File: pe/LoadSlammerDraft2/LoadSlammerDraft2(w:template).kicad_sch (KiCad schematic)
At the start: 14 parts, among them J1 Screw_Terminal_01x02, J2 Conn_Coaxial, J3 Conn_Coaxial, Q1 Q_NMOS_GDS, U1 ${SIM.PARAMS}, U2 BD50FC0FP

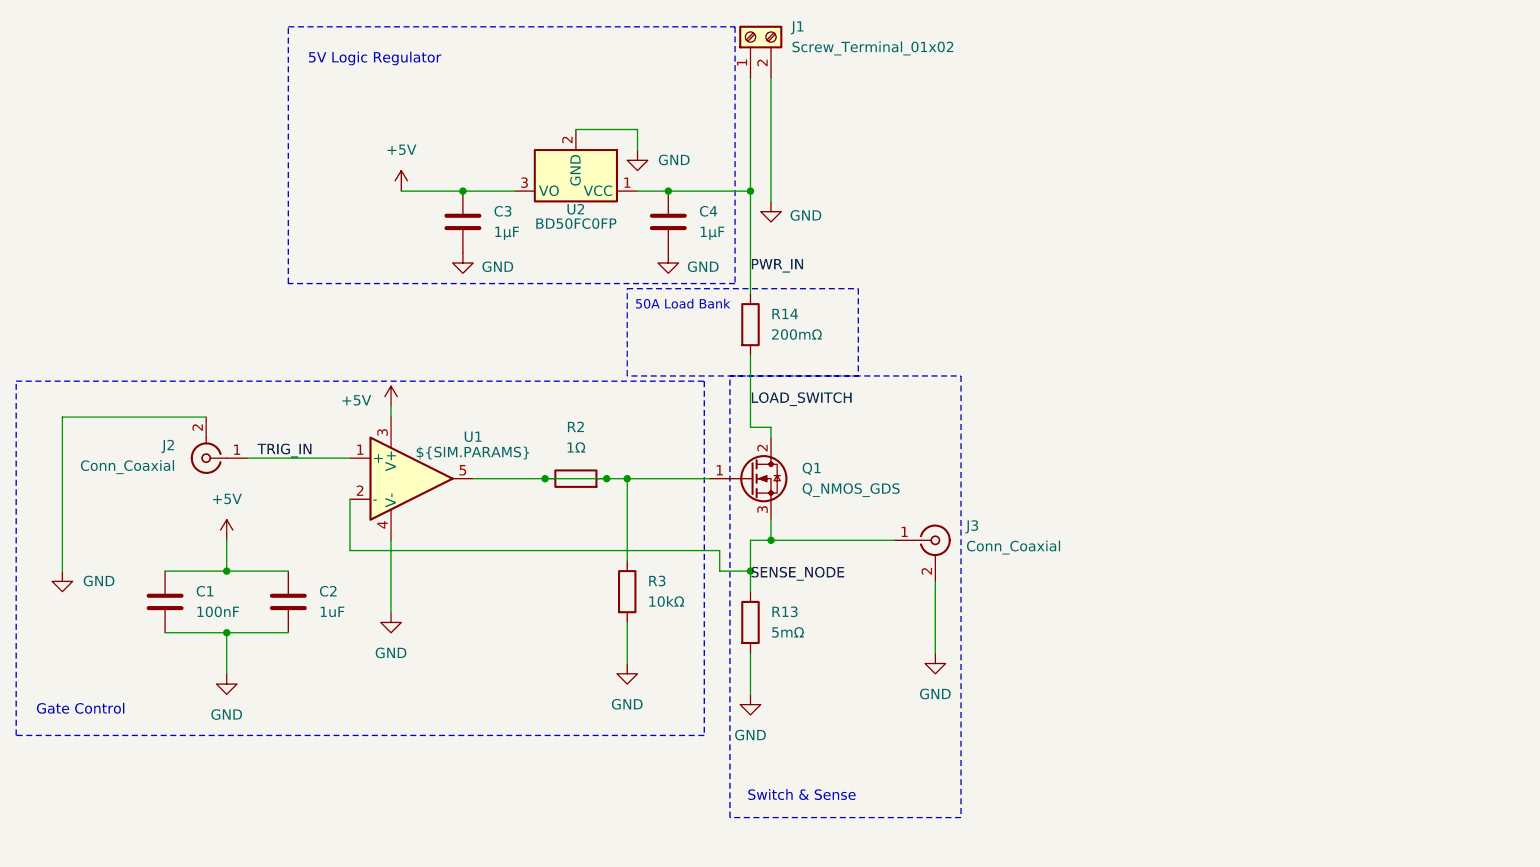
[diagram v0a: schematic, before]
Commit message: Load Slammer: cleaner schematic layout, J2/J3 changed from BNC to 2-pin headers, removed J4
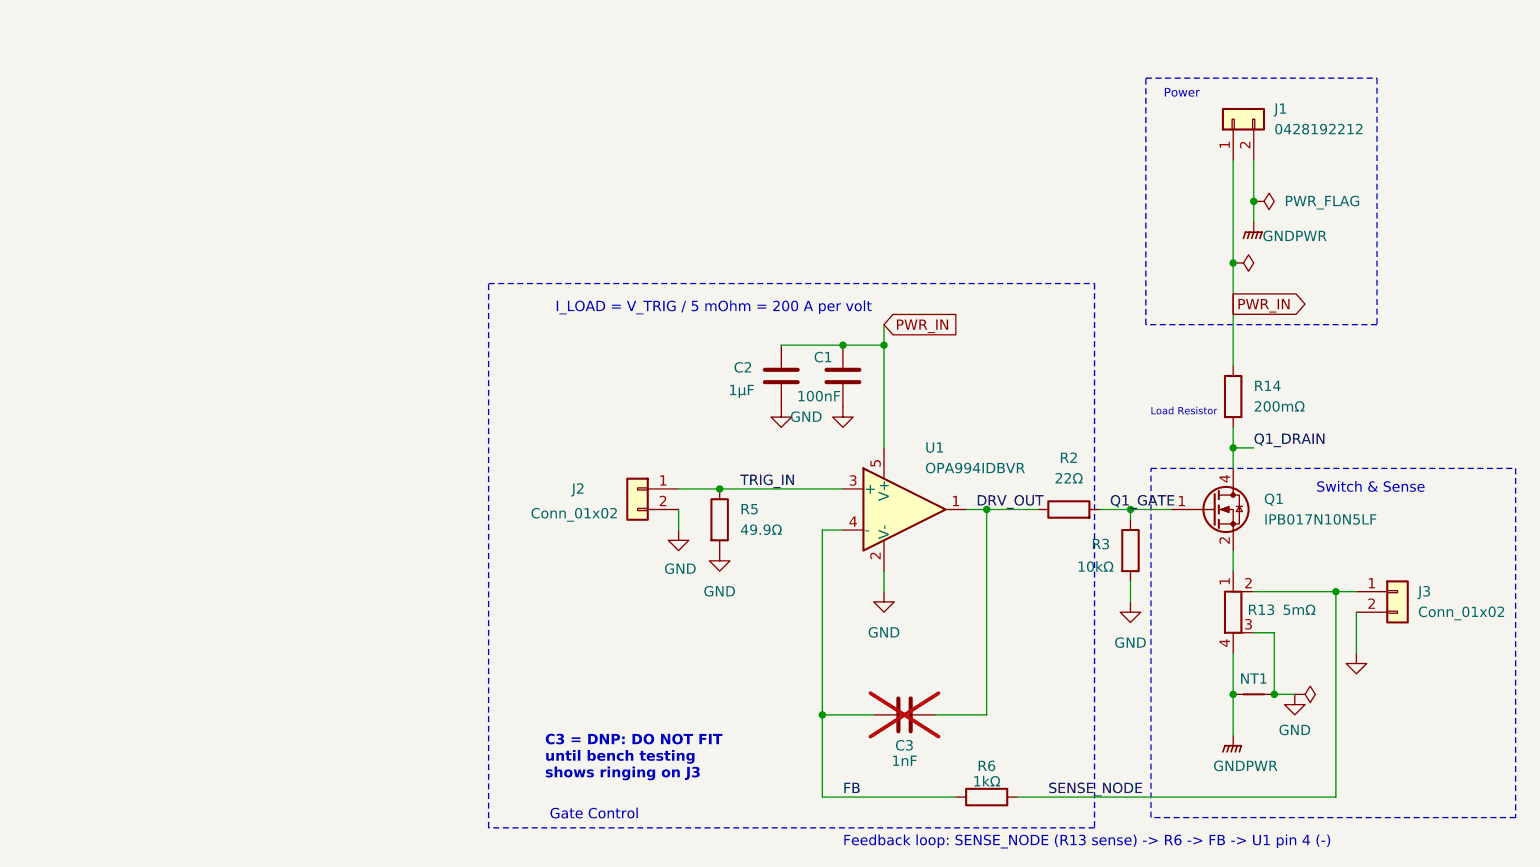
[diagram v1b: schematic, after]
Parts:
- removed C4: 1µF, Package_TO_SOT_SMD:TO-252-2, symbol Device:C
- removed U2: BD50FC0FP, Package_TO_SOT_SMD:TO-252-2, symbol Regulator_Linear:BD50FC0FP
- added NT1: NetTie_2, NetTie:NetTie-2_SMD_Pad0.5mm, symbol Device:NetTie_2
- added R5: 49.9Ω, Resistor_SMD:R_2512_6332Metric_Pad1.40x3.35mm_HandSolder, symbol Device:R
- added R6: 1kΩ, Resistor_SMD:R_0603_1608Metric_Pad0.98x0.95mm_HandSolder, symbol Device:R
- C1: footprint (none) -> Capacitor_SMD:C_0603_1608Metric_Pad1.08x0.95mm_HandSolder; Digikey Part Number (none) -> 311-1344-1-ND; Digikey URL (none) -> https://www.digikey.com/en/products/detail/yageo/CC0603KRX7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; Manufacturer (none) -> YAGEO; Manufacturer Part Number (none) -> CC0603KRX7R9BB104
- C2: value 1uF -> 1µF; footprint (none) -> Capacitor_SMD:C_0603_1608Metric_Pad1.08x0.95mm_HandSolder; Digikey Part Number (none) -> 445-CGA3E3X7R1H105K080ABCT-ND; Digikey URL (none) -> https://www.digikey.com/en/products/detail/tdk-corporation/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; Manufacturer (none) -> TDK; Manufacturer Part Number (none) -> CGA3E3X7R1H105K080AB
- C3: value 1µF -> 1nF; footprint Package_TO_SOT_SMD:TO-252-2 -> Capacitor_SMD:C_0603_1608Metric_Pad1.08x0.95mm_HandSolder; Digikey Part Number (none) -> 490-1451-1-ND; Digikey URL (none) -> https://www.digikey.com/en/products/detail/murata-electroni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; Manufacturer (none) -> Murata Electronics; Manufacturer Part Number (none) -> GRM1885C1H102JA01D; now not fitted
- J1: value Screw_Terminal_01x02 -> 0428192212; footprint (none) -> formula_slug_footprint_library:Molex_Mini-Fit_Sr_42819-22XX_1x02_P10.00mm_Vertical; symbol Connector:Screw_Terminal_01x02 -> Connector_Generic:Conn_01x02; Digikey Part Number (none) -> WM1937-ND; Digikey URL (none) -> https://www.digikey.com/en/products/detail/molex/0428192212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; Manufacturer (none) -> Molex; Manufacturer Part Number (none) -> 0428192212
- J2, J3: value Conn_Coaxial -> Conn_01x02; footprint (none) -> Connector_PinHeader_2.54mm:PinHeader_1x02_P2.54mm_Vertical; symbol Connector:Conn_Coaxial -> Connector_Generic:Conn_01x02
- Q1: value Q_NMOS_GDS -> IPB017N10N5LF; footprint Package_TO_SOT_SMD:SOT-23-6 -> Package_TO_SOT_SMD:TO-263-7_TabPin4; symbol Transistor_FET:Q_NMOS_GDS -> formula_slug_symbol_library:IPB017N10N5LF; Digikey Part Number (none) -> IPB017N10N5LFATMA1CT-ND; Digikey URL (none) -> https://www.digikey.com/en/products/detail/infineon-technol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; Manufacturer (none) -> Infineon Technologies; Manufacturer Part Number (none) -> IPB017N10N5LFATMA1
- R13: footprint (none) -> Resistor_SMD:R_Shunt_Ohmite_LVK25; symbol Device:R -> Device:R_Shunt; Digikey Part Number (none) -> 273-LVK25R005FERCT-ND; Digikey URL (none) -> https://www.digikey.com/en/products/detail/ohmite/LVK25R005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; Manufacturer (none) -> Ohmite; Manufacturer Part Number (none) -> LVK25R005FER
- R14: footprint Package_TO_SOT_THT:TO-247-2_Horizontal_TabDown -> Package_TO_SOT_THT:TO-247-2_Vertical; Digikey Part Number (none) -> 2485-TEH100MR200JE-ND; Digikey URL (none) -> https://www.digikey.com/en/products/detail/ohmite/TEH100MR2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; Manufacturer (none) -> Ohmite
- R2: value 1Ω -> 22Ω; footprint (none) -> Resistor_SMD:R_0603_1608Metric_Pad0.98x0.95mm_HandSolder; Digikey Part Number (none) -> P22.0HCT-ND; Digikey URL (none) -> https://www.digikey.com/en/products/detail/panasonic-electr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; Manufacturer (none) -> Panasonic; Manufacturer Part Number (none) -> ERJ-3EKF22R0V
- R3: footprint (none) -> Resistor_SMD:R_0603_1608Metric_Pad0.98x0.95mm_HandSolder; Digikey Part Number (none) -> P10.0KHCT-ND; Digikey URL (none) -> https://www.digikey.com/en/products/detail/panasonic-electr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; Manufacturer (none) -> Panasonic; Manufacturer Part Number (none) -> ERJ-3EKF1002V
- U1: value ${SIM.PARAMS} -> OPA994IDBVR; footprint Package_TO_SOT_SMD:SOT-353_SC-70-5 -> Package_TO_SOT_SMD:SOT-23-5; symbol Simulation_SPICE:OPAMP -> Amplifier_Operational:OPA365xxDBV; Digikey Part Number (none) -> 296-OPA994IDBVRCT-ND; Digikey URL (none) -> https://www.digikey.com/en/products/detail/texas-instrument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; Manufacturer (none) -> Texas Instruments; Manufacturer Part Number (none) -> OPA994IDBVR
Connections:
- net GND: now also R13.3, U1.2 (V-), NT1.2, R5.2; no longer C3.1, J1.2 (Pin_2), R13.2, U1.4 (V-)
- net PWR_IN: now also C1.1, C2.1, U1.5 (V+)
- net SENSE_NODE: now also R13.2, R6.2; no longer Q1.3 (S), R13.1, U1.2 (-)
- net TRIG_IN: now also U1.3 (+), R5.1; no longer U1.1 (+)
- net Q1_GATE: now reaches Q1.1 (G), R2.2, R3.1
- net Q1_GATE: no longer R2.1, U1.5
- removed net +5V: C1.1, C2.1, C3.2, U1.3 (V+)
- net LOAD_SWITCH: no longer names the net of Q1.2 (S)
- net LOAD_SWITCH: now also Q1.3 (S), Q1.5 (S), Q1.6 (S), Q1.7 (S), R13.1; no longer R14.2
- new net DRV_OUT: C3.2, R2.1, U1.1
- new net FB: C3.1, R6.1, U1.4 (-)
- new net GNDPWR: J1.2 (Pin_2), NT1.1, R13.4
- new net Q1_DRAIN: Q1.4 (D), R14.2
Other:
- note added: "C3 = DNP: DO NOT FIT until bench testing shows ringing on J3"
- note added: "Feedback loop: SENSE_NODE (R13 sense) -> R6 -> FB -> U1 pin 4 (-)"
- note added: "I_LOAD = V_TRIG / 5 mOhm = 200 A per volt"
- note added: "Load Resistor"
- note added: "Power"
- note removed: "50A Load Bank"
- note removed: "5V Logic Regulator"
- moved on the sheet: C1, Q1, R14, R2, R3, U1
